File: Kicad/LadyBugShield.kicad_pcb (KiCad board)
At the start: 2 copper layers, 81.3 x 55.3 mm, 52 parts, among them P1 CONN_6, P2 CONN_2, P3 BNC, P4 BNC, Q1 TIP122, Q2 TIP122, Q3 TIP122, Q4 MOSFET_N, U1 74LVC1G53, U2 MCP6242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

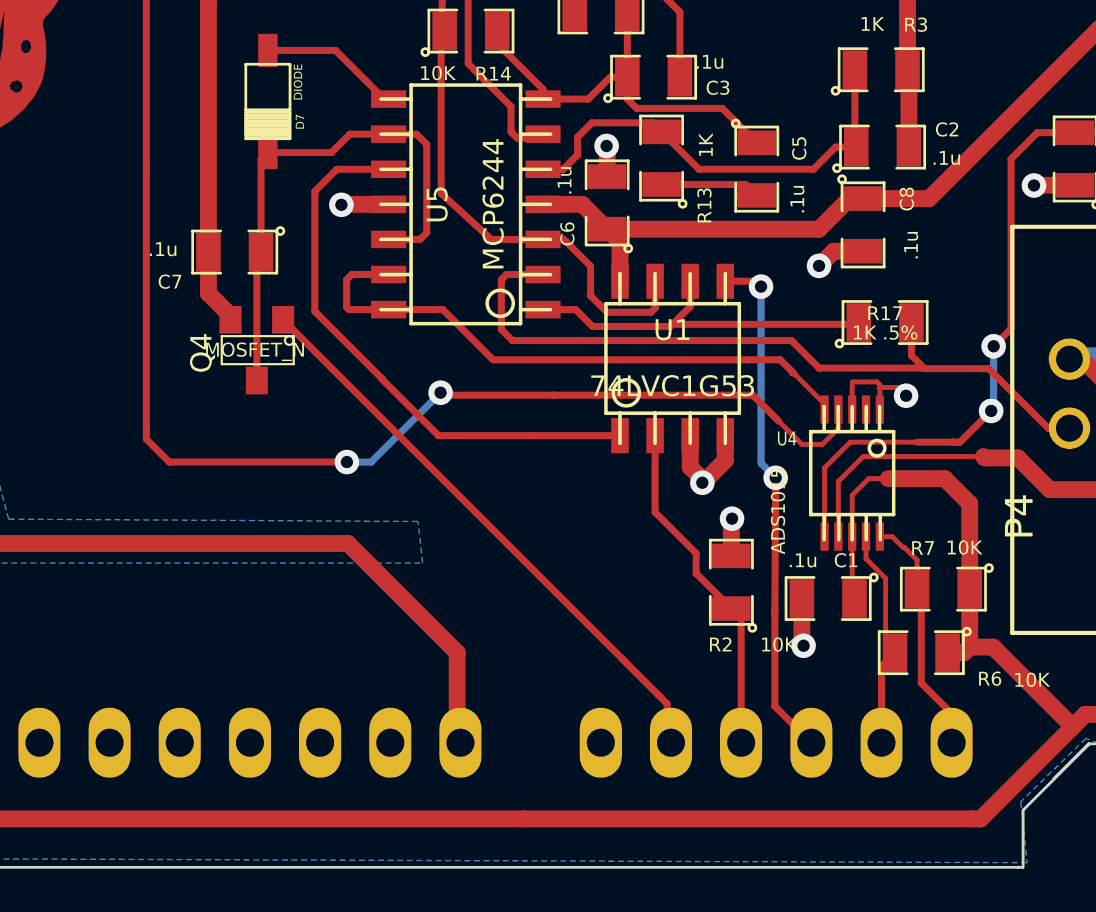
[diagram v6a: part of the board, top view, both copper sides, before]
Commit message: updated layout to fix wrong footprint for TSSOP8
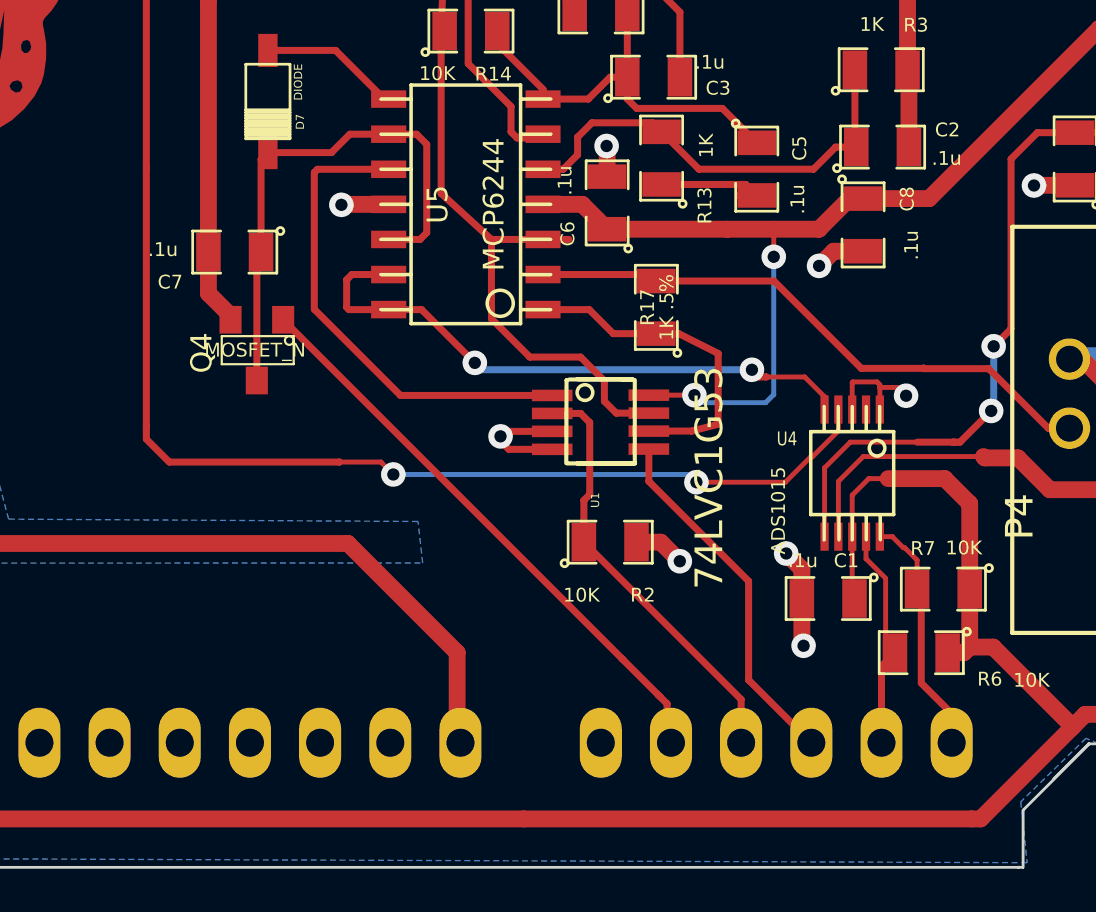
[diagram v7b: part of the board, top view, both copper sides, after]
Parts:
- U1: footprint so-8 -> LB_TSSOP8
- moved R17 8.30 mm to (210.4, 98.5), turned to 90 degrees
- moved R2 4.62 mm to (208.7, 107.0), turned to 0 degrees
- moved U1 2.27 mm to (210.8, 102.6), turned to 270 degrees
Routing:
- net VClean: track 302.5 -> 311.3 mm, vias 0 -> 2
- net /EC/EC_ProbeIN: track 27.3 -> 21.4 mm
- net /Arduino/MUX_out_pin: track 18.8 -> 13.1 mm, vias 2 -> 0
- net /EC/AC/EC_Vin+: track 20.6 -> 25.1 mm
- net /Arduino/MUX_enable_pin: track 12.4 -> 15.5 mm
- net /EC/Rectify/Signal: track 20.6 -> 17.9 mm
- net GND: track 48.0 -> 50.5 mm, vias 18 -> 19
- net /EC/ECGain/EC_DCv: track 13.8 -> 12.0 mm
- net /DigitalAccess/pH_AIN: track 81.9 -> 80.9 mm
- net /DigitalAccess/EC_AIN: track 21.6 -> 21.9 mm, vias 0 -> 2

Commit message: updated layout prior to sending to OshPark
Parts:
- moved C8 8.46 mm to (213.9, 103.0)
- moved R2 2.77 mm to (206.4, 108.5), turned to 180 degrees
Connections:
- R2 pad 2: GND -> VClean
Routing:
- net VClean: track 311.3 -> 320.1 mm
- net /EC/ECGain/EC_DCv: track 12.0 -> 18.3 mm, vias 0 -> 2
- net GND: track 50.5 -> 46.7 mm, vias 19 -> 17
- net /DigitalAccess/pH_AIN: track 80.9 -> 83.6 mm
- net /Arduino/FET_pin: track 21.3 -> 23.4 mm
- net /Arduino/MUX_enable_pin: track 15.5 -> 16.3 mm
